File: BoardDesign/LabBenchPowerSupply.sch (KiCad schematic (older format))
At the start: 52 parts, among them P1 Digital, P2 Analog, P3 CONN_01X01, P4 CONN_01X01, P5 CONN_01X01, P6 CONN_01X01

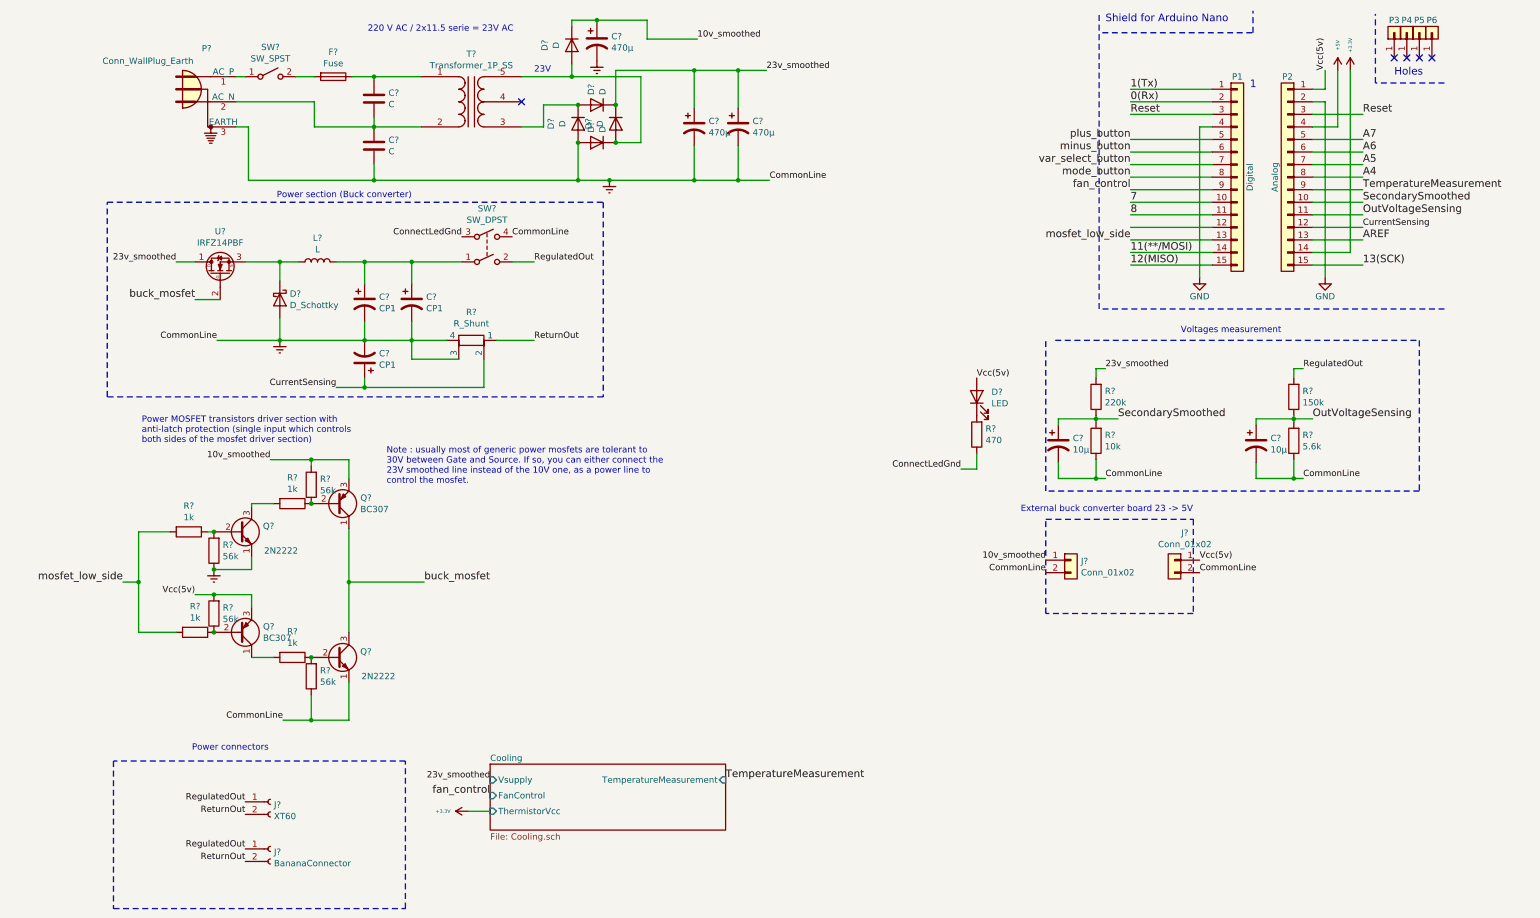
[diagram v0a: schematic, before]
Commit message: Modified labels & driver circuitry
Signed-off-by: bebenlebricolo <benoittarrade@hotmail.fr>
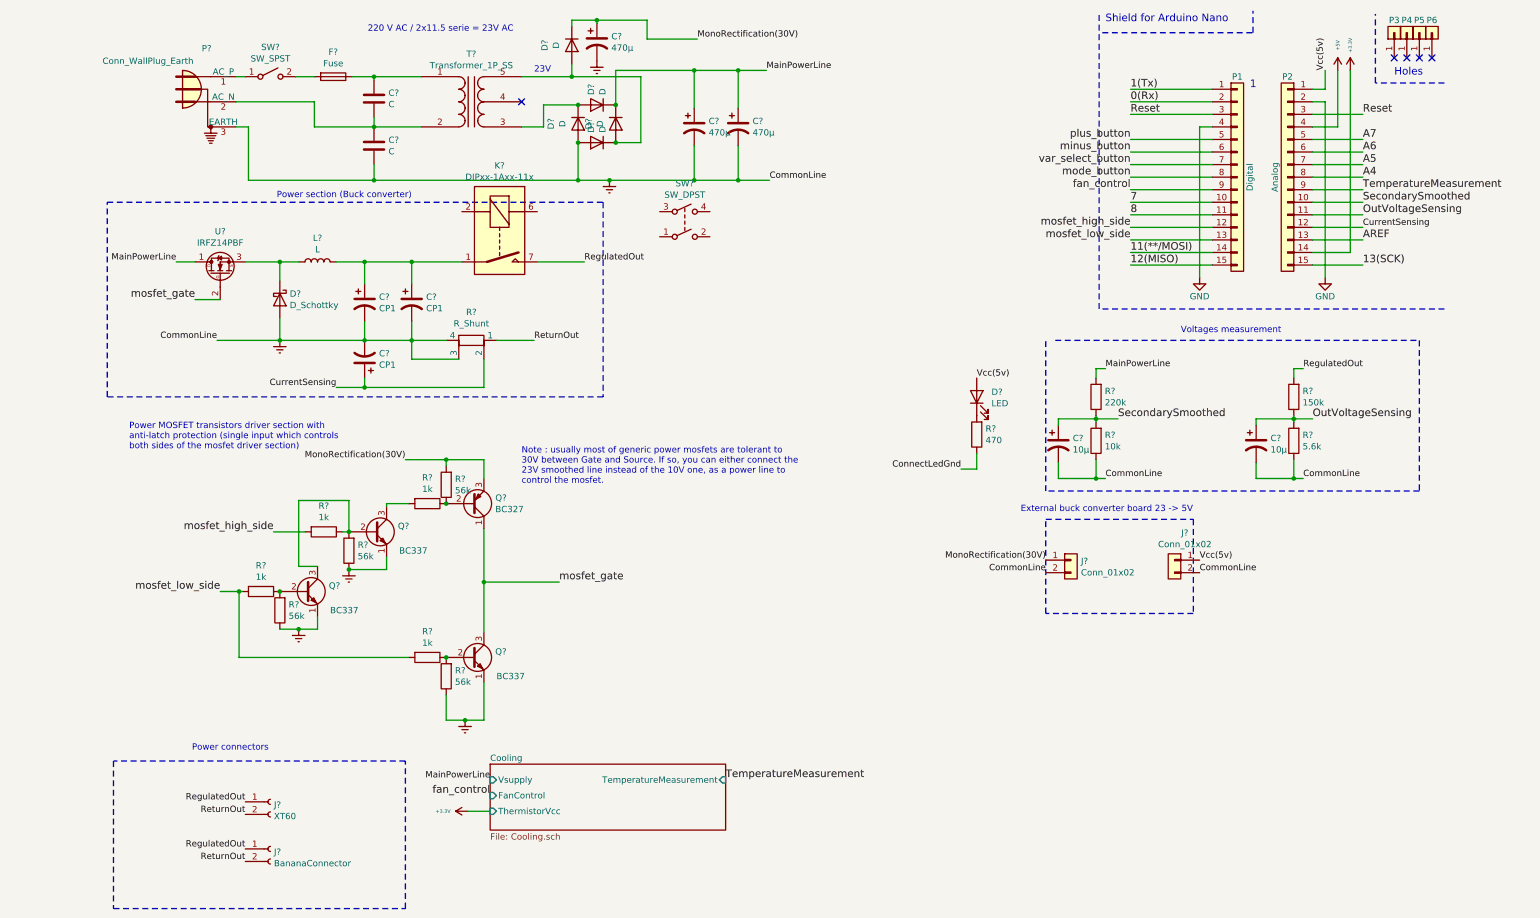
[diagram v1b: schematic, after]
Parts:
- removed Q?: BC307, Package_TO_SOT_THT:TO-92_Inline, symbol Transistor_BJT:BC307
- removed R?: 56k, symbol Device:R
- removed R?: 1k, symbol Device:R
- added K?: DIPxx-1Axx-11x, Relay_THT:Relay_StandexMeder_DIP_LowProfile, symbol Relay:DIPxx-1Axx-11x
- added Q?: BC337, Package_TO_SOT_THT:TO-39-3, symbol Transistor_BJT:2N2219
- added R?: 56k, symbol Device:R
- added R?: 1k, symbol Device:R
- Q?: value BC307 -> BC327
- Q? (x2): value 2N2222 -> BC337
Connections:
- net ConnectLedGnd: no longer SW?.3
- net Earth: now also Q?.1 (E), R?.1; no longer SW?.4
- net RegulatedOut: now also K?.7, K?.8; no longer SW?.2
- net mosfet_low_side: now also R?.2, R?.2; no longer R?.2
- net mosfet_high_side: now reaches P1.12 (Pin_12)
- net mosfet_high_side: now also R?.2
- net at C?.1, C?.1, L?.2: now also K?.1, K?.14; no longer SW?.1
- net at Q?.2 (B), R?.1, R?.2: now also Q?.3 (C)
- net 10v_smoothed renamed MonoRectification(30V)
- net 23v_smoothed renamed MainPowerLine
- net buck_mosfet renamed mosfet_gate
- new net: Q?.2 (B), R?.1, R?.2
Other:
- moved on the sheet: Q?, R?, SW?

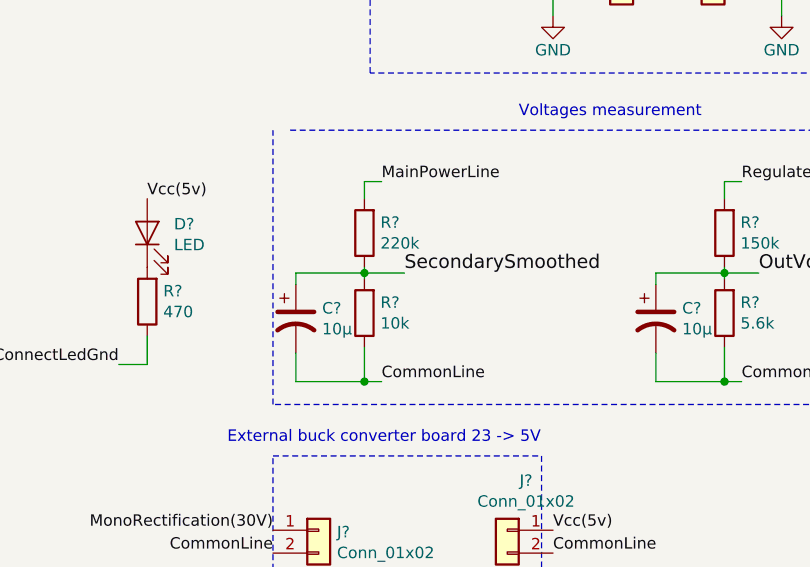
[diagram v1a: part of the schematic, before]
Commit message: Adapted divider bridges to max input 33V
Signed-off-by: bebenlebricolo <benoittarrade@hotmail.fr>
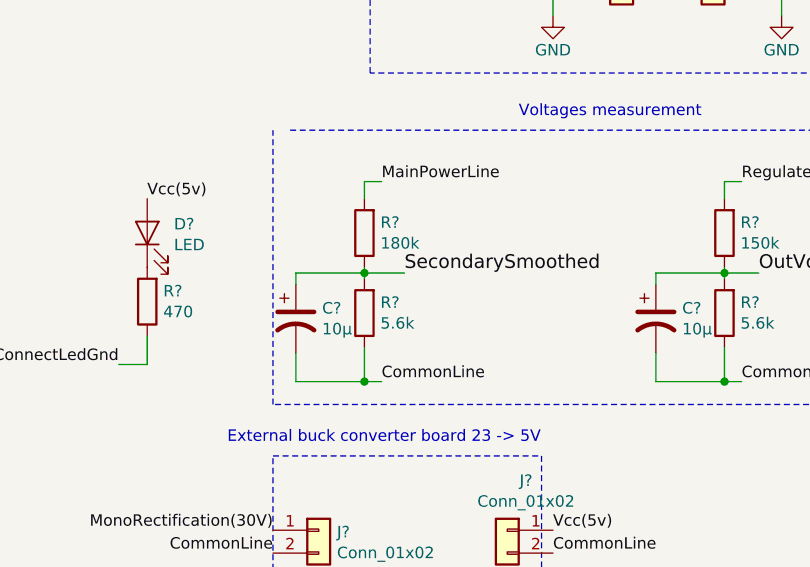
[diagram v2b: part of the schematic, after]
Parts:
- R?: value 220k -> 180k
- R?: value 10k -> 5.6k
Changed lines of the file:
@@
 AR Path="/5EE32D8E/5EE6415A" Ref="R?"  Part="1"
 F 0 "R?" H 8355 3504 50  0000 R CNN
-F 1 "220k" H 8355 3595 50  0000 R CNN
+F 1 "180k" H 8355 3595 50  0000 R CNN
 F 2 "" V 8355 3550 50  0001 C CNN
 F 3 "~" H 8425 3550 50  0001 C CNN
@@
 AR Path="/5EE32D8E/5EE64161" Ref="R?"  Part="1"
 F 0 "R?" H 8355 3854 50  0000 R CNN
-F 1 "10k" H 8355 3945 50  0000 R CNN
+F 1 "5.6k" H 8355 3945 50  0000 R CNN
 F 2 "" V 8355 3900 50  0001 C CNN
 F 3 "~" H 8425 3900 50  0001 C CNN

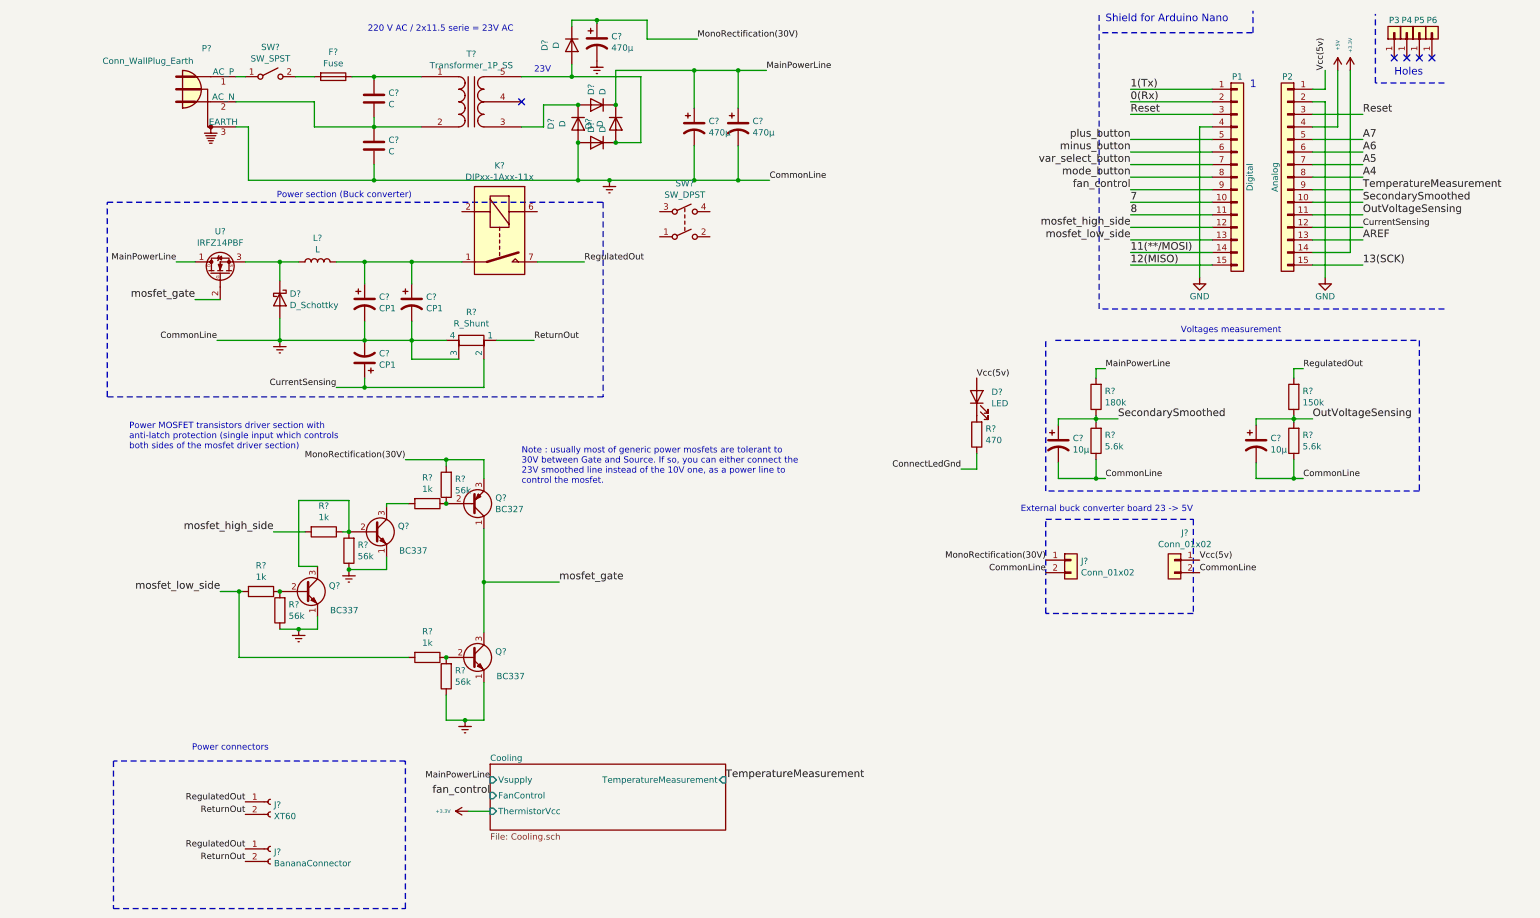
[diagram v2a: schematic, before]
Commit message: Added user-interface buttons wiring
Signed-off-by: bebenlebricolo <benoittarrade@hotmail.fr>
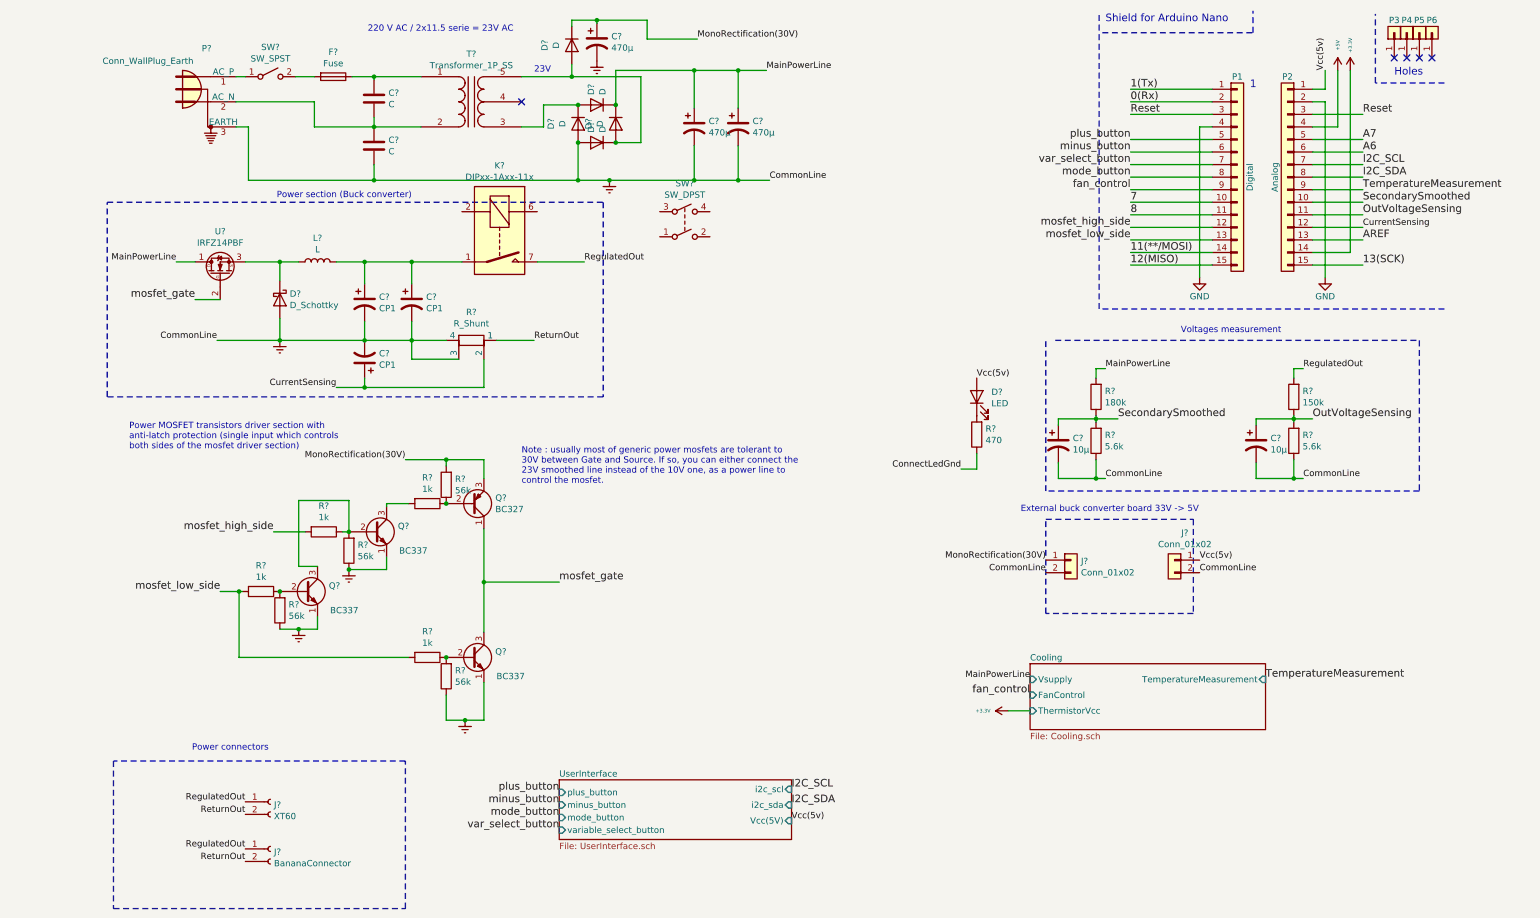
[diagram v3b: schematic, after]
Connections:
- net A4 renamed I2C_SDA
- net A5 renamed I2C_SCL
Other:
- note added: "External buck converter board 33V -> 5V"
- note removed: "External buck converter board 23 -> 5V"
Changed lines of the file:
@@
 $Descr A4 11693 8268
 encoding utf-8
-Sheet 1 2
+Sheet 1 3
 Title "Lab bench power supply"
 Date "2020-03-25"
@@
 TemperatureMeasurement
 Text Label 10550 1800 0    60   ~ 0
-A4
+I2C_SDA
 Text Label 10550 1700 0    60   ~ 0
-A5
+I2C_SCL
 Text Label 10550 1600 0    60   ~ 0
 A6
@@
 	1250 2775 1450 2775
 $Sheet
-S 3600 6475 1875 525
+S 7900 5675 1875 525
 U 5EC77F4C
 F0 "Cooling" 50
 F1 "Cooling.sch" 50
-F2 "FanControl" I L 3600 6725 50
-F3 "ThermistorVcc" I L 3600 6850 50
-F4 "TemperatureMeasurement" I R 5475 6600 50
-F5 "Vsupply" I L 3600 6600 50
+F2 "FanControl" I L 7900 5925 50
+F3 "ThermistorVcc" I L 7900 6050 50
+F4 "TemperatureMeasurement" I R 9775 5800 50
+F5 "Vsupply" I L 7900 5800 50
 $EndSheet
-Text Label 3600 6725 2    60   ~ 0
+Text Label 7900 5925 2    60   ~ 0
 fan_control
 $Comp
@@
 L power:+3V3 #PWR?
 U 1 1 5EFD4716
-P 3425 6850
-F 0 "#PWR?" H 3425 6700 50  0001 C CNN
-F 1 "+3.3V" V 3425 7050 28  0000 C CNN
-F 2 "" H 3425 6850 50  0000 C CNN
-F 3 "" H 3425 6850 50  0000 C CNN
-	1    3425 6850
+P 7725 6050
+F 0 "#PWR?" H 7725 5900 50  0001 C CNN
+F 1 "+3.3V" V 7725 6250 28  0000 C CNN
+F 2 "" H 7725 6050 50  0000 C CNN
+F 3 "" H 7725 6050 50  0000 C CNN
+	1    7725 6050
 	0    -1   -1   0
 $EndComp
 Wire Wire Line
-	3425 6850 3600 6850
-Text Label 5475 6600 0    60   ~ 0
+	7725 6050 7900 6050
+Text Label 9775 5800 0    60   ~ 0
 TemperatureMeasurement
 Text Notes 725  3975 0    50   ~ 0
@@
 	8025 5275 8025 4525
 Text Notes 7825 4475 0    50   ~ 0
-External buck converter board 23 -> 5V
+External buck converter board 33V -> 5V
 Text Label 9250 4850 0    50   ~ 0
 Vcc(5v)
@@
 Text Label 8025 4850 2    50   ~ 0
 MonoRectification(30V)
-Text Label 3600 6600 2    50   ~ 0
+Text Label 7900 5800 2    50   ~ 0
 MainPowerLine
 Text Notes 3850 4250 0    50   ~ 0
@@
 Wire Wire Line
 	3400 6125 3550 6125
+$Sheet
+S 4150 6600 1850 475
+U 5E85D9C1
+F0 "UserInterface" 50
+F1 "UserInterface.sch" 50
+F2 "minus_button" I L 4150 6800 50
+F3 "plus_button" I L 4150 6700 50
+F4 "variable_select_button" I L 4150 7000 50
+F5 "mode_button" I L 4150 6900 50
+F6 "Vcc(5V)" I R 6000 6925 50
+F7 "i2c_sda" I R 6000 6800 50
+F8 "i2c_scl" I R 6000 6675 50
+$EndSheet
+Text Label 4150 6700 2    60   ~ 0
+plus_button
+Text Label 4150 6800 2    60   ~ 0
+minus_button
+Text Label 4150 7000 2    60   ~ 0
+var_select_button
+Text Label 4150 6900 2    60   ~ 0
+mode_button
+Text Label 6000 6675 0    60   ~ 0
+I2C_SCL
+Text Label 6000 6800 0    60   ~ 0
+I2C_SDA
+Text Label 6000 6925 0    50   ~ 0
+Vcc(5v)
 $EndSCHEMATC

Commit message: Adapted schematic to parallel transformer's secondary
Signed-off-by: bebenlebricolo <benoittarrade@hotmail.fr>
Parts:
- removed K?: DIPxx-1Axx-11x, Relay_THT:Relay_StandexMeder_DIP_LowProfile, symbol Relay:DIPxx-1Axx-11x
- removed T?: Transformer_1P_SS, symbol Device:Transformer_1P_SS
- added T?: Transformer_1P_2S, symbol Device:Transformer_1P_2S
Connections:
- net at C?.1, F?.1: now also T?.1 (AA)
- net at C?.1, C?.2, P?.2 (AC_N): now also T?.2 (AB)
- net at D?.1 (K), D?.2 (A): now also T?.4 (SB), T?.6 (SD)
- net at D?.1 (K), D?.2 (A), D?.2 (A): now also T?.3 (SA), T?.5 (SC)
- net MonoRectification(30V) renamed MonoRectification(16V)
- no-connect marks 5 -> 4
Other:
- note added: "220 V AC / 2x11.5 parallel\n* 12V AC / 16V DC rectified"
- note added: "Anti collision protection circuit:\nwhen both high and low lines are triggered, \nthis transistor pulls back to ground the base of high side \nnpn driver, resulting in the extinction of high side driver, \nleaving low side driver on alone (forces N mosfets to close.\nMust reverse logic if P Mosfet is used instead of a N one)"
- note added: "Note : mosfet could either be of N or P type\nN type will not get until full potential but is often \ncheaper, P type can maximise output potential (vout = vin)"
- note added: "Note : usually most of generic power mosfets are tolerant to \naround 20/30V between Gate and Source. \nIf so, you can use the secondary rectified smoothed line \nas the reference voltage to drive the mosfet gate.\nOtherwise, another power supply line (e.g. 12V line) \nwould be necessary and extra care will be required \nin the aim to drive mosfets in their safe area"
- note removed: "220 V AC / 2x11.5 serie = 23V AC"
- note removed: "23V"
- note removed: "Note : usually most of generic power mosfets are tolerant to \n30V between Gate and Source. If so, you can either connect the \n23V smoothed line instead of the 10V one, as a power line to \ncontrol the mosfet."
- moved on the sheet: C?, D?

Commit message: Added a mounting sticking base for all racks
Signed-off-by: bebenlebricolo <benoittarrade@hotmail.fr>
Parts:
- L?: value L -> 110uH
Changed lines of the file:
@@
 P 2225 2475
 F 0 "L?" V 2415 2475 50  0000 C CNN
-F 1 "L" V 2324 2475 50  0000 C CNN
+F 1 "110uH" V 2324 2475 50  0000 C CNN
 F 2 "" H 2225 2475 50  0001 C CNN
 F 3 "~" H 2225 2475 50  0001 C CNN
